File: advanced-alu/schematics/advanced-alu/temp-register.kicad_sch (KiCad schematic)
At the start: 5 parts, among them U16 74LS173, U17 74LS245, U18 74LS173

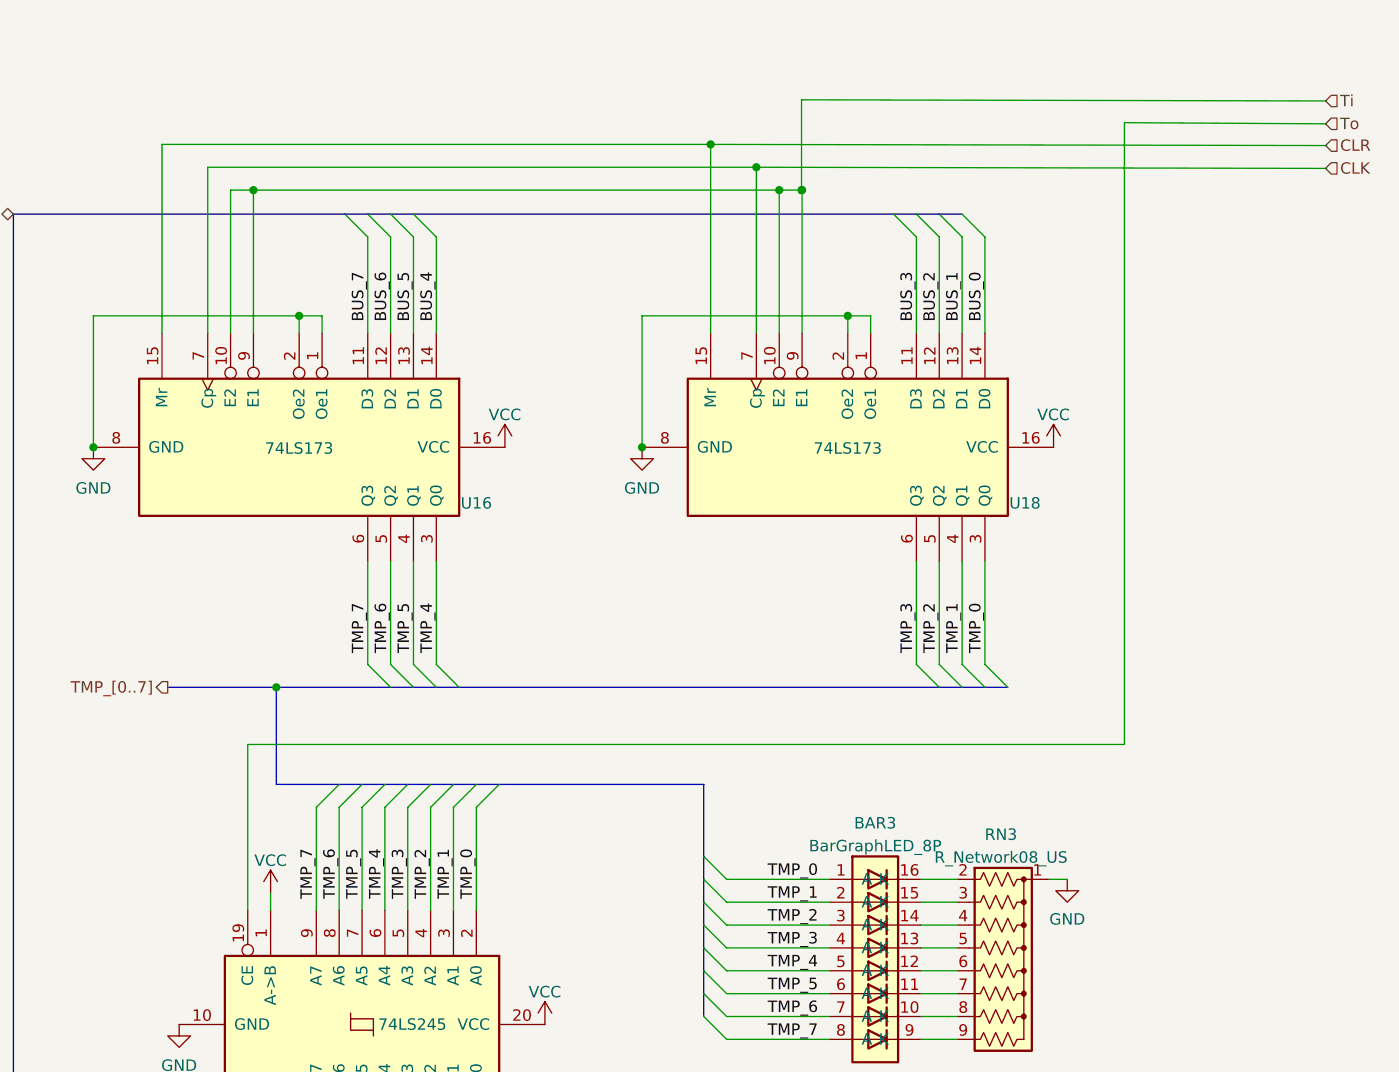
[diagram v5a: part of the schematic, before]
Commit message: corrected control lines
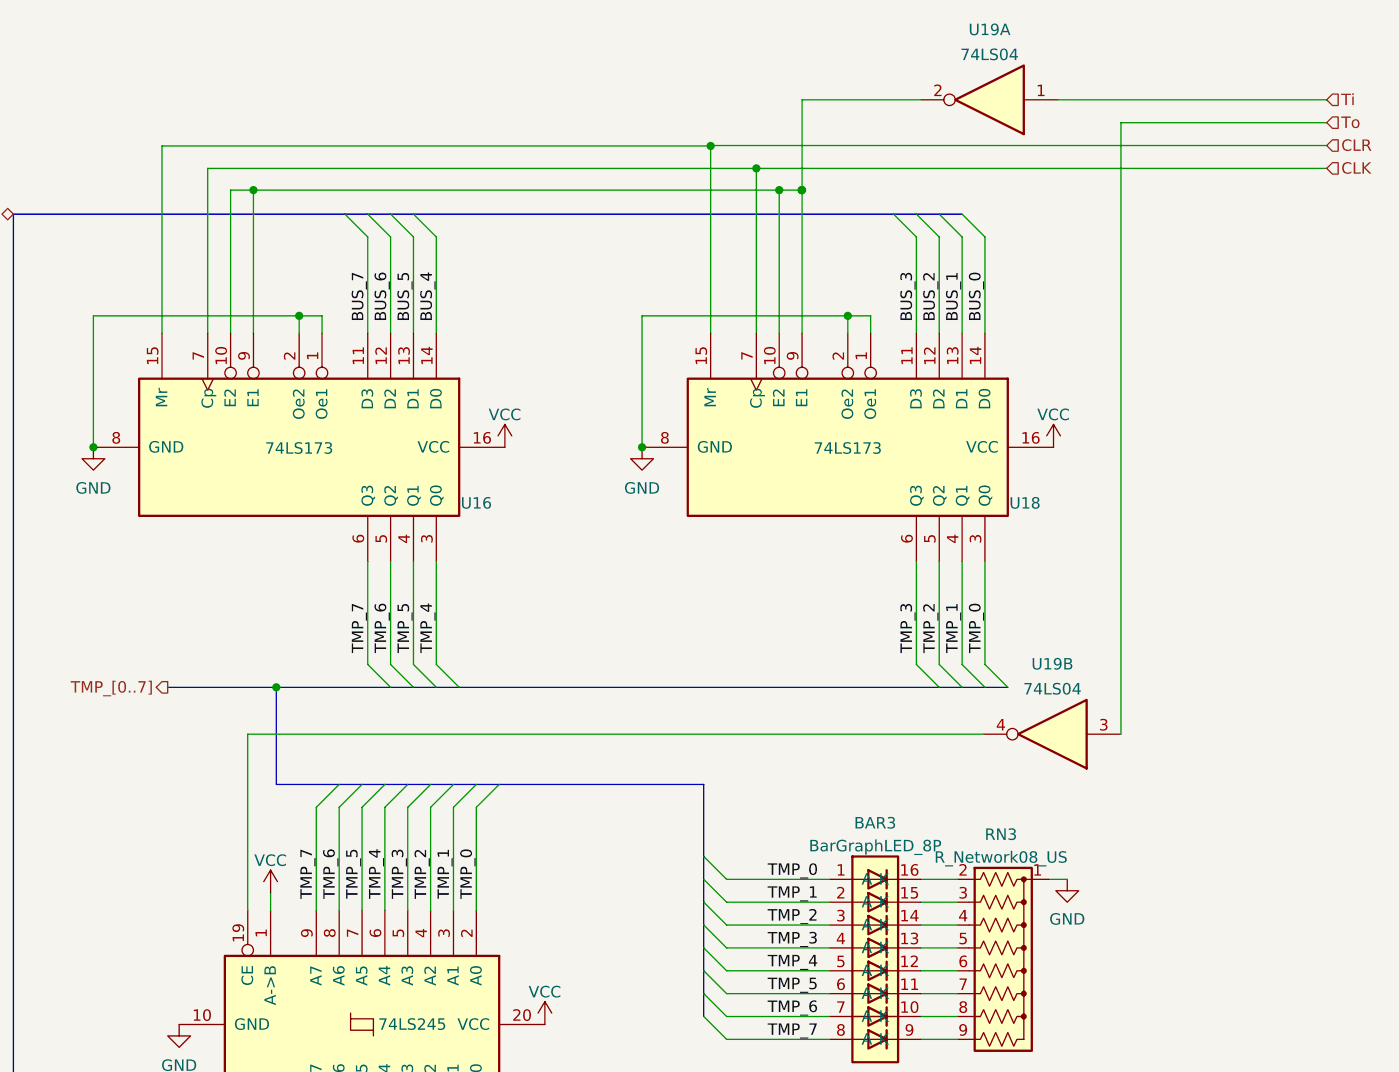
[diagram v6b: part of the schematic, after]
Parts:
- added U19: 74LS04, symbol 74xx:74LS04
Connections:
- net Ti: now also U19.1; no longer U16.10 (E2), U16.9 (E1), U18.10 (E2), U18.9 (E1)
- net To: now also U19.3; no longer U17.19 (CE)
- new net: U16.10 (E2), U16.9 (E1), U18.10 (E2), U18.9 (E1), U19.2
- new net: U17.19 (CE), U19.4
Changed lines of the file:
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@@
     (title "Advanced Arithmetic Logic Unit - Temp Register")
   )
-  (junction (at 159.512 41.783) (diameter 0) (color 0 0 0 0)
-  )
   (junction (at 90.932 75.438) (diameter 0) (color 0 0 0 0)
   )
   (junction (at 174.752 60.833) (diameter 0) (color 0 0 0 0)
   )
+  (junction (at 159.512 41.9577) (diameter 0) (color 0 0 0 0)
+  )
+  (junction (at 169.672 46.863) (diameter 0) (color 0 0 0 0)
+  )
   (junction (at 108.712 46.863) (diameter 0) (color 0 0 0 0)
   )
-  (junction (at 164.592 44.323) (diameter 0) (color 0 0 0 0)
-  )
   (junction (at 167.132 46.863) (diameter 0) (color 0 0 0 0)
   )
@@
   (junction (at 151.892 75.438) (diameter 0) (color 0 0 0 0)
   )
+  (junction (at 164.592 44.45) (diameter 0) (color 0 0 0 0)
+  )
   (junction (at 169.6115 46.863) (diameter 0) (color 0 0 0 0)
   )
-  (junction (at 169.672 46.863) (diameter 0) (color 0 0 0 0)
-  )
   (bus_entry (at 130.937 112.903) (size -2.54 2.54)
     (stroke (width 0) (type default) (color 0 0 0 0))
@@
     (stroke (width 0) (type default) (color 0 0 0 0))
   )
+  (wire (pts (xy 159.512 41.9577) (xy 98.552 41.9577))
+    (stroke (width 0) (type default) (color 0 0 0 0))
+  )
   (bus (pts (xy 118.237 112.903) (xy 120.777 112.903))
     (stroke (width 0) (type default) (color 0 0 0 0))
@@
     (stroke (width 0) (type default) (color 0 0 0 0))
   )
+  (wire (pts (xy 164.592 44.45) (xy 103.632 44.45))
+    (stroke (width 0) (type default) (color 0 0 0 0))
+  )
   (bus (pts (xy 184.912 102.108) (xy 131.572 102.108))
     (stroke (width 0) (type default) (color 0 0 0 0))
   )
-  (wire (pts (xy 169.6115 36.83) (xy 169.6115 46.863))
-    (stroke (width 0) (type default) (color 0 0 0 0))
-  )
   (bus (pts (xy 123.317 112.903) (xy 125.857 112.903))
     (stroke (width 0) (type default) (color 0 0 0 0))
@@
     (stroke (width 0) (type default) (color 0 0 0 0))
   )
+  (wire (pts (xy 198.12 36.83) (xy 227.965 36.83))
+    (stroke (width 0) (type default) (color 0 0 0 0))
+  )
   (wire (pts (xy 115.697 152.273) (xy 115.697 161.798))
     (stroke (width 0) (type default) (color 0 0 0 0))
@@
     (stroke (width 0) (type default) (color 0 0 0 0))
   )
+  (wire (pts (xy 159.512 41.9577) (xy 159.512 62.738))
+    (stroke (width 0) (type default) (color 0 0 0 0))
+  )
+  (wire (pts (xy 227.965 44.45) (xy 164.592 44.45))
+    (stroke (width 0) (type default) (color 0 0 0 0))
+  )
   (wire (pts (xy 177.292 60.833) (xy 174.752 60.833))
     (stroke (width 0) (type default) (color 0 0 0 0))
@@
     (stroke (width 0) (type default) (color 0 0 0 0))
   )
-  (wire (pts (xy 159.512 41.783) (xy 98.552 41.783))
-    (stroke (width 0) (type default) (color 0 0 0 0))
-  )
   (wire (pts (xy 118.237 152.273) (xy 118.237 161.798))
     (stroke (width 0) (type default) (color 0 0 0 0))
   )
-  (wire (pts (xy 159.512 41.783) (xy 159.512 62.738))
+  (wire (pts (xy 159.512 41.91) (xy 159.512 41.9577))
     (stroke (width 0) (type default) (color 0 0 0 0))
   )
@@
     (stroke (width 0) (type default) (color 0 0 0 0))
   )
-  (wire (pts (xy 159.512 41.783) (xy 227.838 41.91))
+  (wire (pts (xy 182.88 36.83) (xy 169.672 36.83))
+    (stroke (width 0) (type default) (color 0 0 0 0))
+  )
+  (wire (pts (xy 205.105 39.37) (xy 205.105 107.315))
     (stroke (width 0) (type default) (color 0 0 0 0))
   )
@@
     (stroke (width 0) (type default) (color 0 0 0 0))
   )
+  (wire (pts (xy 227.965 41.91) (xy 159.512 41.91))
+    (stroke (width 0) (type default) (color 0 0 0 0))
+  )
+  (wire (pts (xy 227.965 39.37) (xy 205.105 39.37))
+    (stroke (width 0) (type default) (color 0 0 0 0))
+  )
   (wire (pts (xy 189.992 88.138) (xy 189.992 99.568))
     (stroke (width 0) (type default) (color 0 0 0 0))
@@
     (stroke (width 0) (type default) (color 0 0 0 0))
   )
-  (wire (pts (xy 227.838 39.497) (xy 205.486 39.37))
-    (stroke (width 0) (type default) (color 0 0 0 0))
-  )
-  (wire (pts (xy 205.486 39.37) (xy 205.486 108.458))
-    (stroke (width 0) (type default) (color 0 0 0 0))
-  )
   (wire (pts (xy 106.172 46.863) (xy 106.172 62.738))
     (stroke (width 0) (type default) (color 0 0 0 0))
@@
     (stroke (width 0) (type default) (color 0 0 0 0))
   )
+  (wire (pts (xy 103.632 44.45) (xy 103.632 62.738))
+    (stroke (width 0) (type default) (color 0 0 0 0))
+  )
   (bus (pts (xy 182.372 49.53) (xy 184.912 49.53))
     (stroke (width 0) (type default) (color 0 0 0 0))
@@
     (stroke (width 0) (type default) (color 0 0 0 0))
   )
-  (wire (pts (xy 108.077 108.458) (xy 108.077 126.873))
+  (wire (pts (xy 169.672 36.83) (xy 169.672 46.863))
+    (stroke (width 0) (type default) (color 0 0 0 0))
+  )
+  (wire (pts (xy 108.077 107.315) (xy 108.077 126.873))
     (stroke (width 0) (type default) (color 0 0 0 0))
   )
@@
     (stroke (width 0) (type default) (color 0 0 0 0))
   )
-  (wire (pts (xy 108.077 108.458) (xy 205.486 108.458))
-    (stroke (width 0) (type default) (color 0 0 0 0))
-  )
   (wire (pts (xy 189.992 52.07) (xy 189.992 62.738))
     (stroke (width 0) (type default) (color 0 0 0 0))
@@
     (stroke (width 0) (type default) (color 0 0 0 0))
   )
-  (wire (pts (xy 98.552 41.783) (xy 98.552 62.738))
-    (stroke (width 0) (type default) (color 0 0 0 0))
-  )
   (bus (pts (xy 123.952 49.53) (xy 126.492 49.53))
     (stroke (width 0) (type default) (color 0 0 0 0))
@@
     (stroke (width 0) (type default) (color 0 0 0 0))
   )
-  (wire (pts (xy 103.632 44.323) (xy 103.632 62.738))
+  (wire (pts (xy 164.592 44.45) (xy 164.592 62.738))
     (stroke (width 0) (type default) (color 0 0 0 0))
   )
@@
     (stroke (width 0) (type default) (color 0 0 0 0))
   )
-  (wire (pts (xy 227.838 36.957) (xy 169.6115 36.83))
-    (stroke (width 0) (type default) (color 0 0 0 0))
-  )
   (wire (pts (xy 123.317 126.873) (xy 123.317 115.443))
     (stroke (width 0) (type default) (color 0 0 0 0))
@@
     (stroke (width 0) (type default) (color 0 0 0 0))
   )
-  (wire (pts (xy 164.592 44.323) (xy 164.592 62.738))
-    (stroke (width 0) (type default) (color 0 0 0 0))
-  )
   (bus (pts (xy 136.017 112.903) (xy 158.75 112.903))
     (stroke (width 0) (type default) (color 0 0 0 0))
@@
     (stroke (width 0) (type default) (color 0 0 0 0))
   )
+  (wire (pts (xy 189.865 107.315) (xy 108.077 107.315))
+    (stroke (width 0) (type default) (color 0 0 0 0))
+  )
   (bus (pts (xy 121.412 49.53) (xy 123.952 49.53))
     (stroke (width 0) (type default) (color 0 0 0 0))
@@
     (stroke (width 0) (type default) (color 0 0 0 0))
   )
+  (wire (pts (xy 98.552 41.9577) (xy 98.552 62.738))
+    (stroke (width 0) (type default) (color 0 0 0 0))
+  )
   (bus (pts (xy 120.777 164.338) (xy 118.237 164.338))
     (stroke (width 0) (type default) (color 0 0 0 0))
@@
     (stroke (width 0) (type default) (color 0 0 0 0))
   )
-  (wire (pts (xy 164.592 44.323) (xy 103.632 44.323))
-    (stroke (width 0) (type default) (color 0 0 0 0))
-  )
   (bus (pts (xy 131.572 102.108) (xy 129.032 102.108))
     (stroke (width 0) (type default) (color 0 0 0 0))
@@
     (stroke (width 0) (type default) (color 0 0 0 0))
   )
-  (wire (pts (xy 164.592 44.323) (xy 227.838 44.45))
-    (stroke (width 0) (type default) (color 0 0 0 0))
-  )
   (wire (pts (xy 172.72 125.984) (xy 161.29 125.984))
     (stroke (width 0) (type default) (color 0 0 0 0))
@@
     (effects (font (size 1.27 1.27)) (justify left bottom))
   )
-  (hierarchical_label "CLK" (shape input) (at 227.838 44.45 0)
+  (hierarchical_label "CLK" (shape input) (at 227.965 44.45 0)
     (effects (font (size 1.27 1.27)) (justify left))
   )
-  (hierarchical_label "CLR" (shape input) (at 227.838 41.91 0)
+  (hierarchical_label "CLR" (shape input) (at 227.965 41.91 0)
     (effects (font (size 1.27 1.27)) (justify left))
   )
@@
     (effects (font (size 1.27 1.27)) (justify right))
   )
-  (hierarchical_label "Ti" (shape input) (at 227.838 36.957 0)
+  (hierarchical_label "Ti" (shape input) (at 227.965 36.83 0)
     (effects (font (size 1.27 1.27)) (justify left))
   )
-  (hierarchical_label "To" (shape input) (at 227.838 39.497 0)
+  (hierarchical_label "To" (shape input) (at 227.965 39.37 0)
     (effects (font (size 1.27 1.27)) (justify left))
   )
@@
     (pin "1")
   )
+  (symbol (lib_id "74xx:74LS04") (at 190.5 36.83 180) (unit 1)
+    (in_bom yes) (on_board yes) (fields_autoplaced)
+    (property "Reference" "U19" (id 0) (at 190.5 29.0535 0))
+    (property "Value" "74LS04" (id 1) (at 190.5 31.8286 0))
+    (property "Footprint" "" (id 2) (at 190.5 36.83 0)
+      (effects (font (size 1.27 1.27)) hide)
+    )
+    (property "Datasheet" "http://www.ti.com/lit/gpn/sn74LS04" (id 3) (at 190.5 36.83 0)
+      (effects (font (size 1.27 1.27)) hide)
+    )
+    (pin "1")
+    (pin "2")
+  )
   (symbol (lib_id "Device:R_Network08_US") (at 192.024 133.604 270) (unit 1)
     (in_bom yes) (on_board yes) (fields_autoplaced)
@@
     (pin "9")
   )
+  (symbol (lib_id "74xx:74LS04") (at 197.485 107.315 180) (unit 2)
+    (in_bom yes) (on_board yes) (fields_autoplaced)
+    (property "Reference" "U19" (id 0) (at 197.485 99.5385 0))
+    (property "Value" "74LS04" (id 1) (at 197.485 102.3136 0))
+    (property "Footprint" "" (id 2) (at 197.485 107.315 0)
+      (effects (font (size 1.27 1.27)) hide)
+    )
+    (property "Datasheet" "http://www.ti.com/lit/gpn/sn74LS04" (id 3) (at 197.485 107.315 0)
+      (effects (font (size 1.27 1.27)) hide)
+    )
+    (pin "3")
+    (pin "4")
+  )
   (symbol (lib_id "power:VCC") (at 110.617 124.968 0) (unit 1)
